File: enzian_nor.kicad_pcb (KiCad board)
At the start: 4 copper layers, 75 x 60 mm, 27 parts, among them IC1 L7809ABD2T-TR, J1 ASP-134488-01, U1 MT35XU02GCBA1G12-0AUT

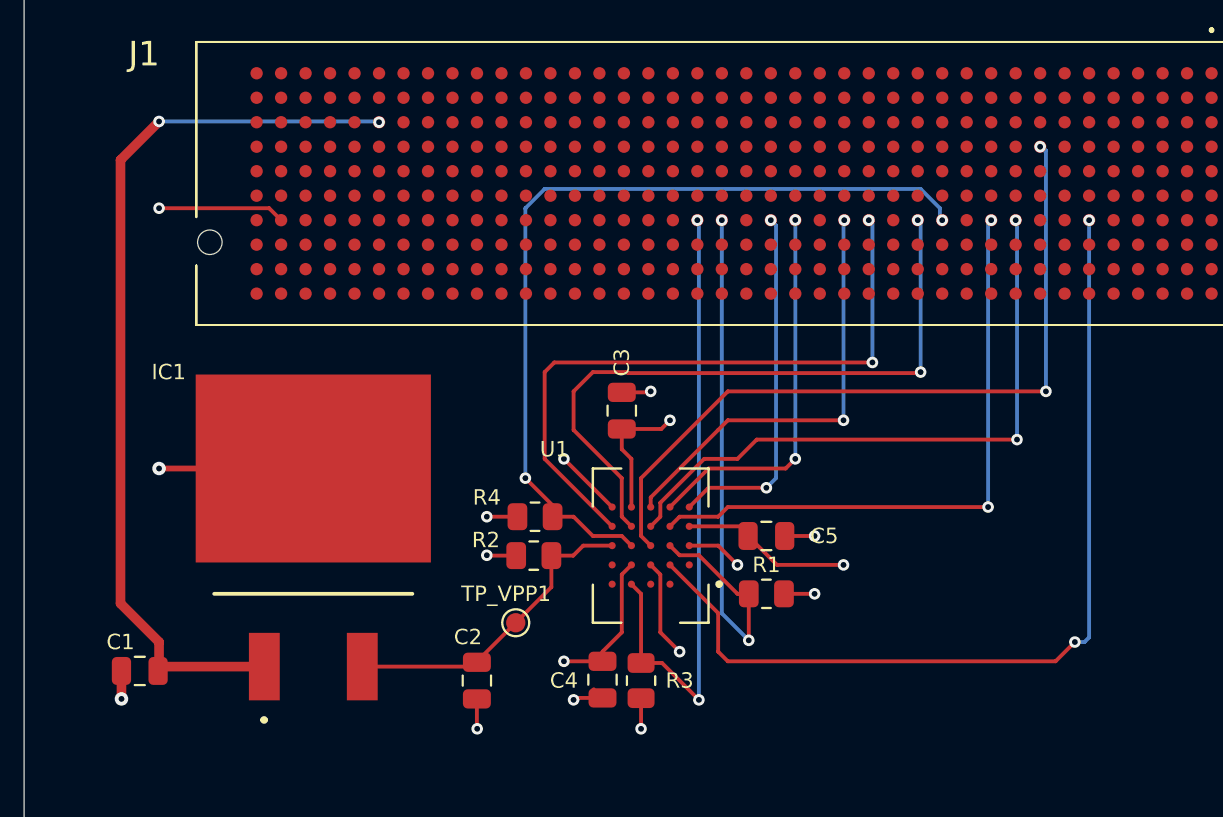
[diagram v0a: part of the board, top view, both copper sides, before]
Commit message: Update vias to diagonal positions to match the enzian main board
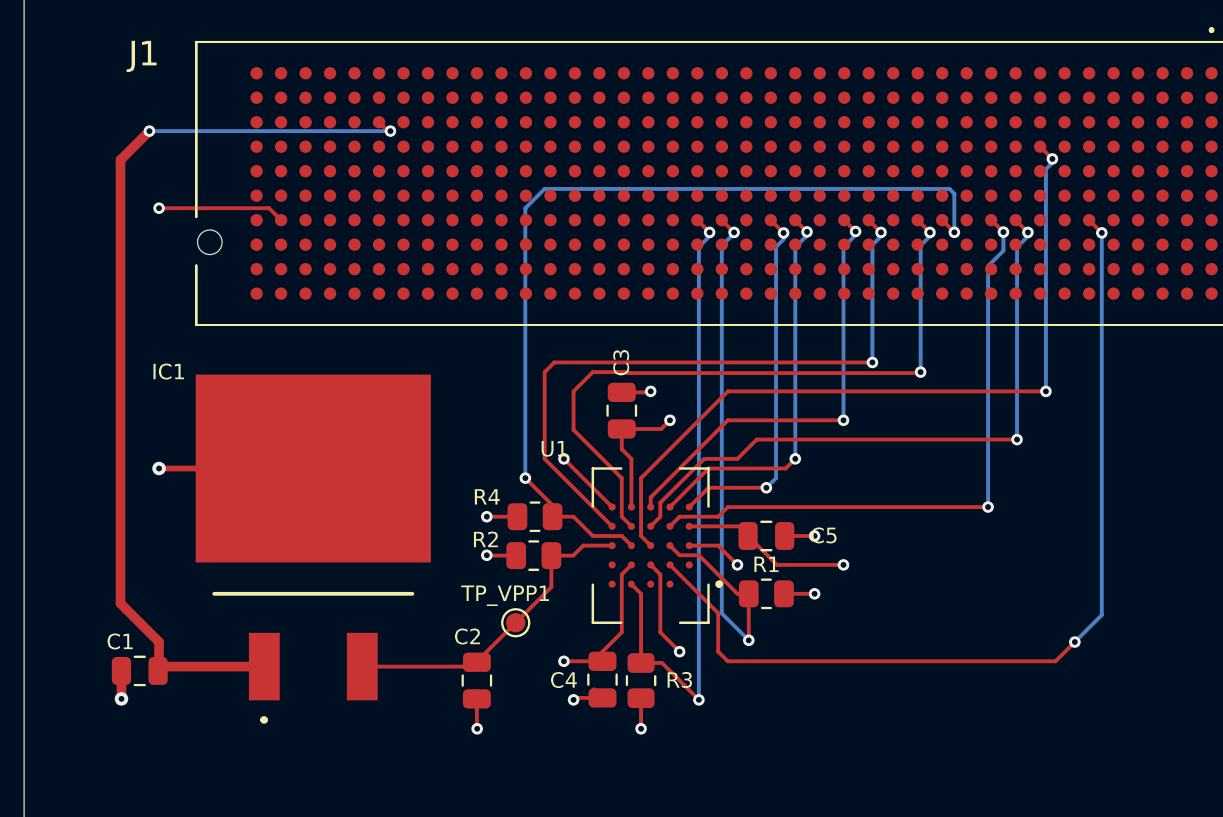
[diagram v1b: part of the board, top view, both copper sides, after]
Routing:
- net /NOR_DQ2: track 44.3 -> 47.1 mm
- net /12V_PSUP: track 47.3 -> 48.4 mm
- net /NOR_DQ1: track 31.9 -> 32.6 mm
- net /NOR_S#: track 30.0 -> 30.6 mm

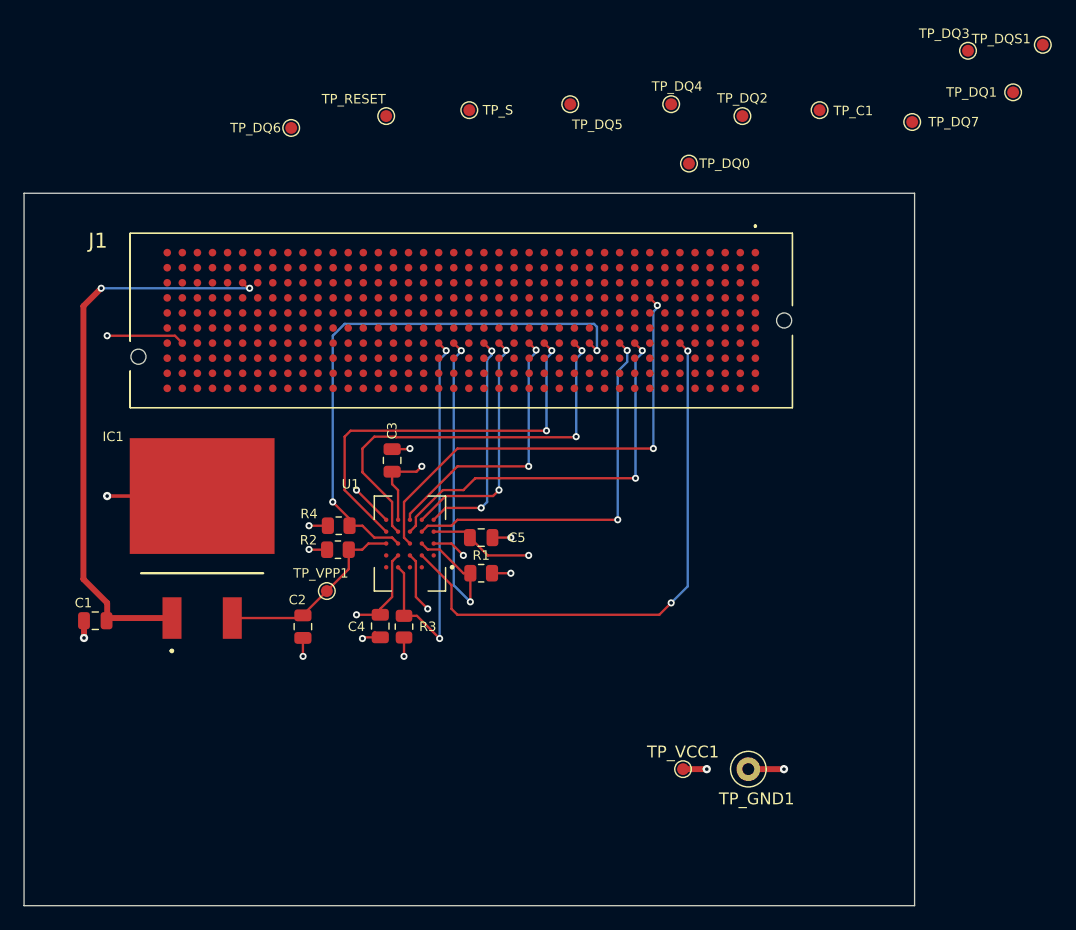
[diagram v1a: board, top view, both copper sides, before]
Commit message: Change trace width to 0.35mm/0.5mm for control/power traces, and connected test pads
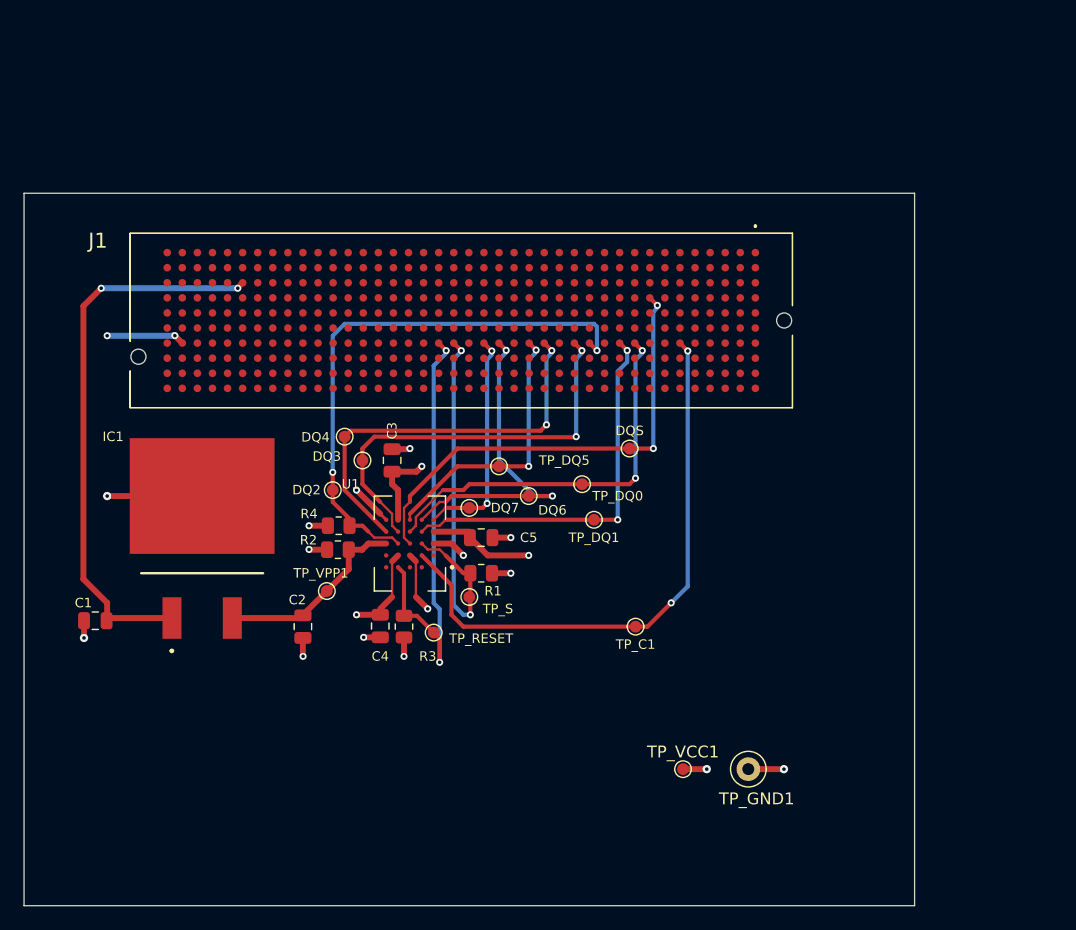
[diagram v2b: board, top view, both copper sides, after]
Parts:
- moved DQ3 61.6 mm to (44.5, 102.0)
- moved TP_DQ1 50.4 mm to (64.0, 107.0)
- moved DQ7 49.5 mm to (53.5, 106.0)
- moved DQS 48.7 mm to (67.0, 101.0)
- moved DQ2 46.7 mm to (42.0, 104.5)
- moved TP_C1 46.2 mm to (67.5, 116.0)
- moved TP_RESET 43.7 mm to (50.5, 116.5)
- moved TP_S 41.0 mm to (53.5, 113.5)
- moved DQ4 39.2 mm to (43.0, 100.0)
- moved DQ6 36.9 mm to (58.5, 105.0)
- moved TP_DQ5 31.1 mm to (56.0, 102.5)
- moved TP_DQ0 28.5 mm to (63.0, 104.0)
- renumbered TP_DQ2 to DQ2, TP_DQ3 to DQ3, TP_DQ4 to DQ4, TP_DQ6 to DQ6, TP_DQ7 to DQ7, TP_DQS1 to DQS
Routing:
- net /NOR_DQ6: track 20.4 -> 28.0 mm
- net /NOR_RESET#: track 33.5 -> 37.9 mm
- net /NOR_S#: track 30.6 -> 34.0 mm
- net /12V_PSUP: track 48.4 -> 47.2 mm
- net /NOR_C: track 47.4 -> 48.5 mm
- net VCC: vias 8 -> 9

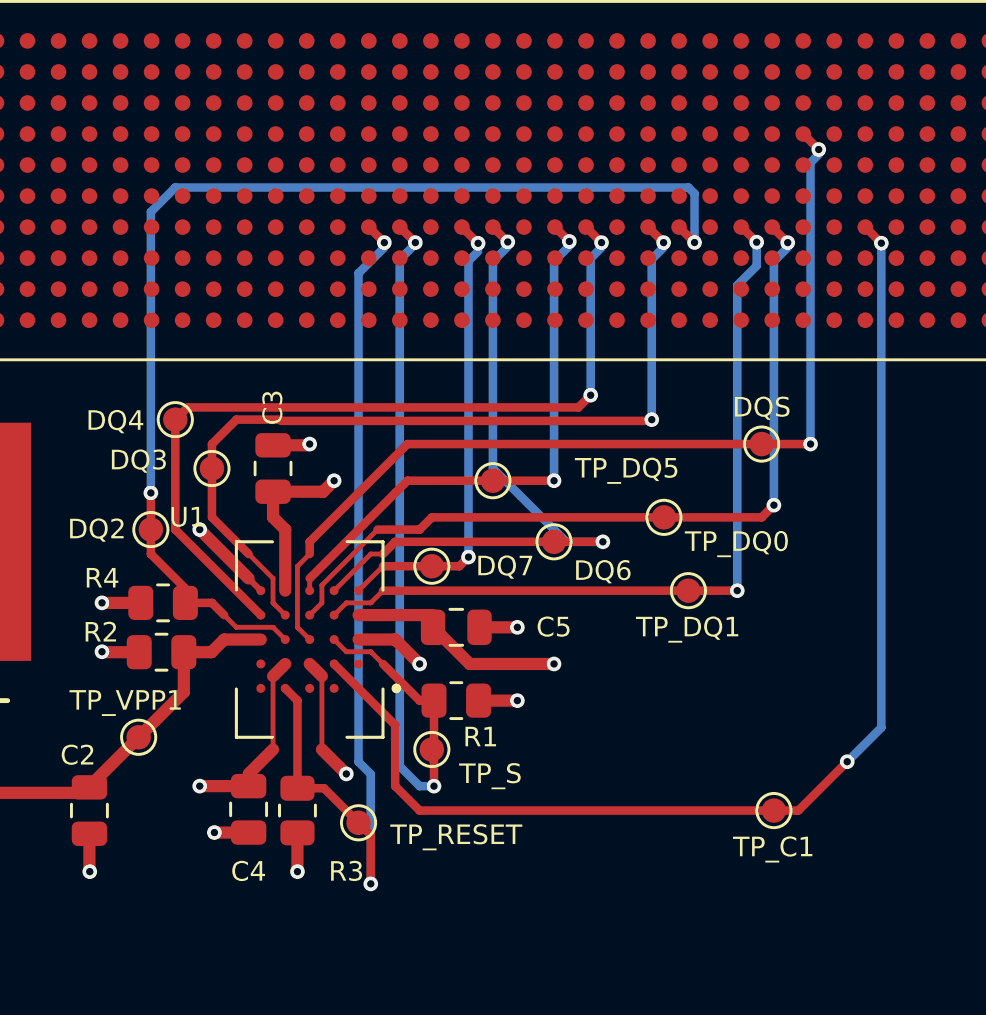
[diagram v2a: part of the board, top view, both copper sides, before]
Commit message: Match trace lengths for all control signals (DQ0-7, C, S#)
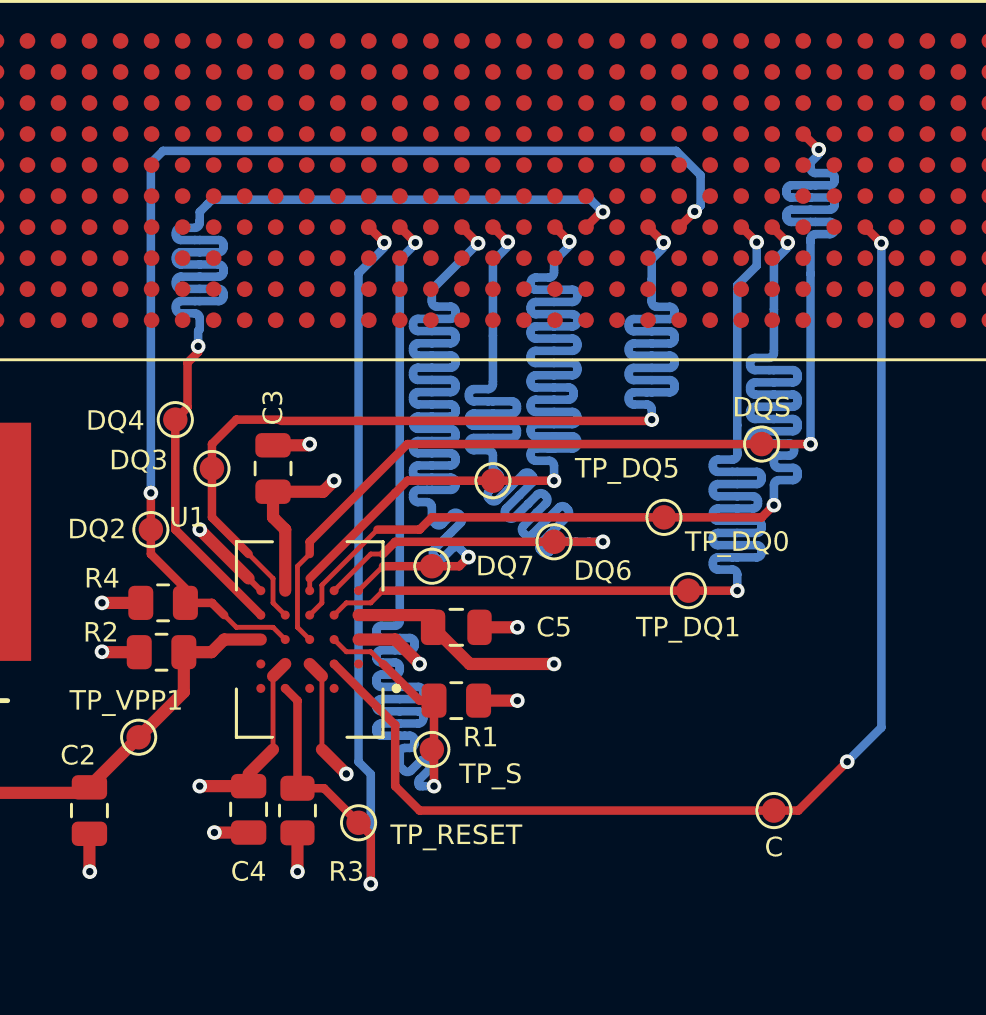
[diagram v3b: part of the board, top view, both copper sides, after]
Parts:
- renumbered TP_C1 to C
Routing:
- net /NOR_DQ7: track 19.0 -> 48.2 mm
- net /NOR_DQ5: track 23.0 -> 48.3 mm
- net /NOR_DQ6: track 28.0 -> 48.3 mm
- net /NOR_DQ1: track 32.6 -> 48.4 mm
- net /NOR_S#: track 34.0 -> 49.3 mm
- net /NOR_DQ0: track 33.2 -> 48.3 mm
- net /NOR_DQ4: track 34.2 -> 48.5 mm
- net /NOR_DQ3: track 35.0 -> 48.4 mm
- net /NOR_DQS: track 39.7 -> 48.4 mm
- net /NOR_DQ2: track 47.1 -> 49.1 mm

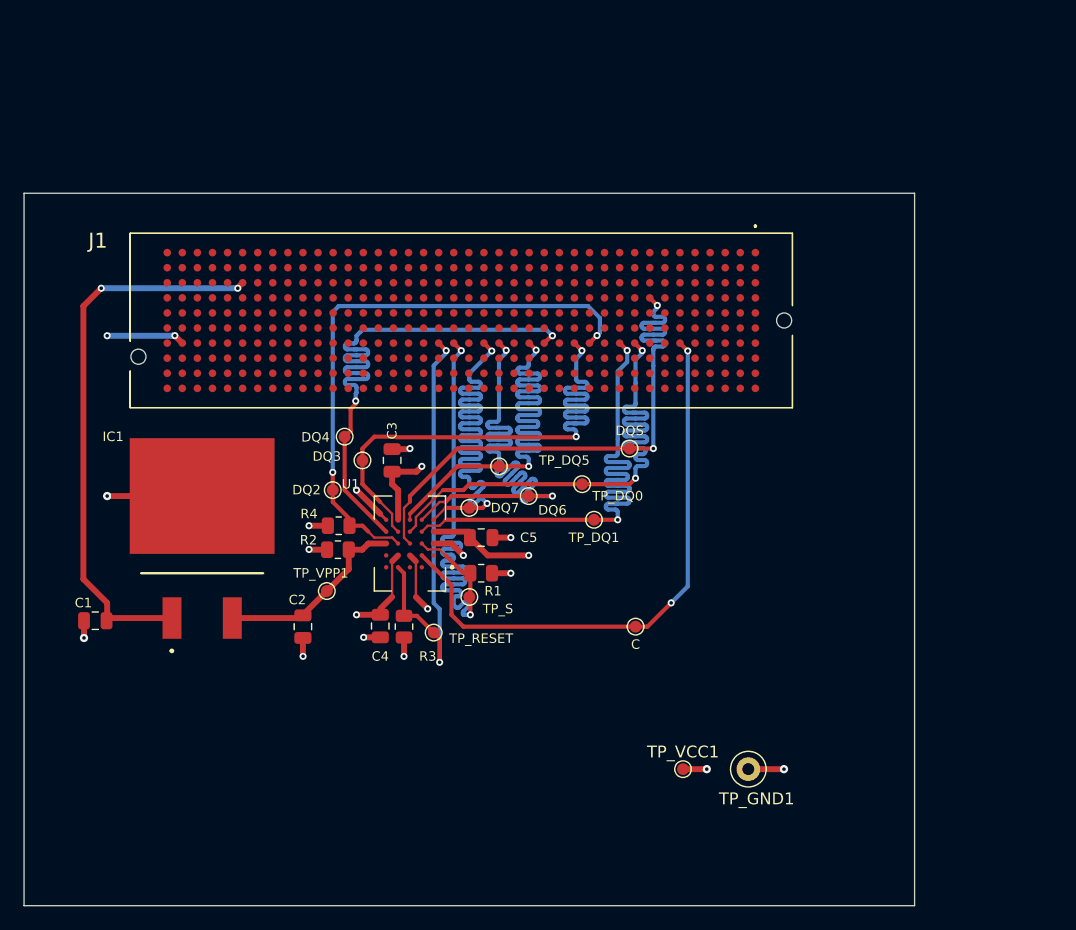
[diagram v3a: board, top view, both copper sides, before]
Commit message: Pour coplanarground plane on the front copper
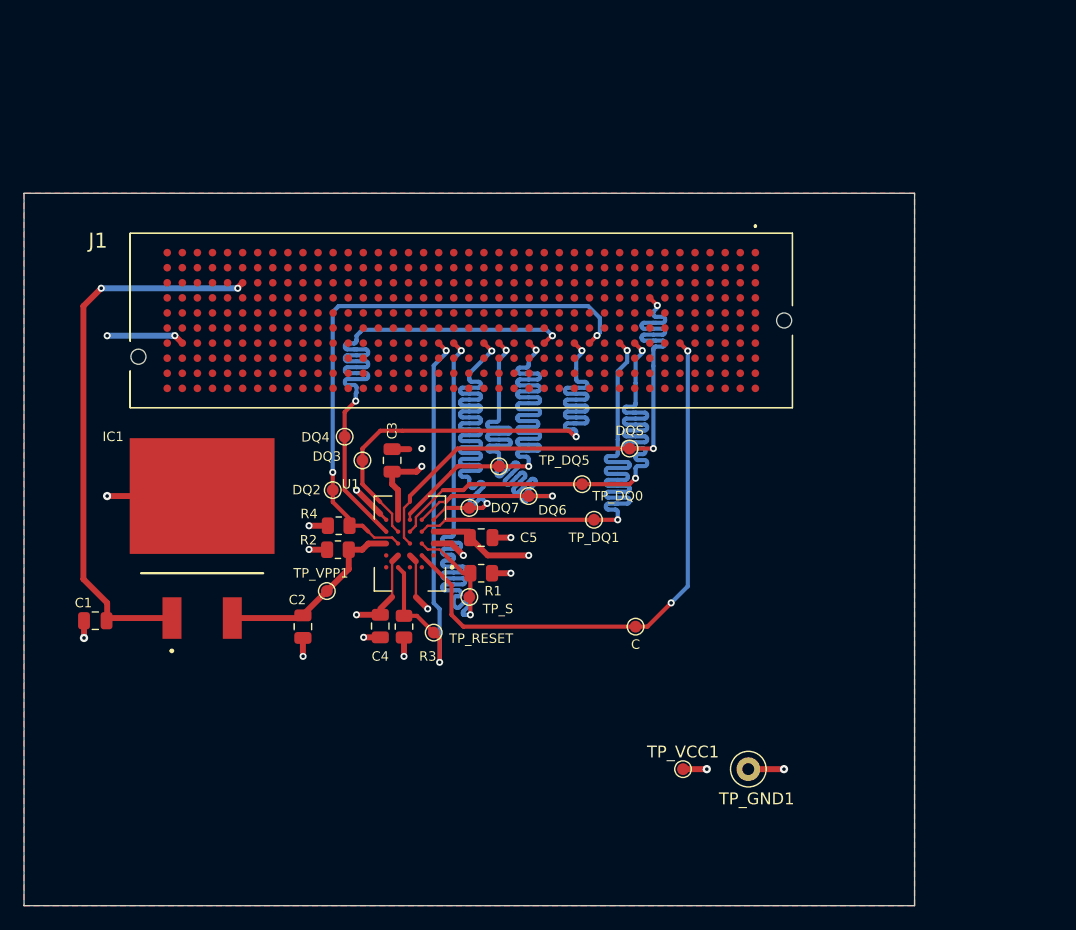
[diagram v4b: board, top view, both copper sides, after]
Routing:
- added copper zone on F.Cu, net GND
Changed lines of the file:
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@@
 	)
 	(segment
-		(start 46 105.5)
-		(end 44.5 104)
+		(start 46 99.5)
+		(end 47.872548 99.5)
 		(width 0.35)
 		(layer "F.Cu")
@@
 	)
 	(segment
-		(start 45.5 100)
-		(end 47.270548 100)
+		(start 61.898 99.5)
+		(end 62.449 100.051)
 		(width 0.35)
 		(layer "F.Cu")
@@
 	)
 	(segment
-		(start 47.270548 100)
-		(end 47.321548 100.051)
+		(start 47 106.5)
+		(end 46 105.5)
 		(width 0.2)
 		(layer "F.Cu")
@@
 	)
 	(segment
-		(start 47.321548 100.051)
-		(end 62.449 100.051)
+		(start 47.872548 99.5)
+		(end 61.898 99.5)
 		(width 0.35)
 		(layer "F.Cu")
@@
 	)
 	(segment
-		(start 44.5 104)
-		(end 44.5 101)
+		(start 44.5 101)
+		(end 46 99.5)
 		(width 0.35)
 		(layer "F.Cu")
@@
 	)
 	(segment
-		(start 47 106.5)
-		(end 46 105.5)
-		(width 0.2)
-		(layer "F.Cu")
-		(net 392)
-	)
-	(segment
-		(start 44.5 101)
-		(end 45.5 100)
+		(start 62.984999 92.754999)
+		(end 62.35 92.12)
 		(width 0.35)
 		(layer "F.Cu")
@@
 	)
 	(segment
-		(start 62.984999 92.754999)
-		(end 62.35 92.12)
+		(start 46 105.5)
+		(end 44.5 104)
 		(width 0.35)
 		(layer "F.Cu")
@@
 	)
 	(segment
+		(start 44.5 104)
+		(end 44.5 101)
+		(width 0.35)
+		(layer "F.Cu")
+		(net 392)
+	)
+	(segment
 		(start 62.449 100.051)
 		(end 62.5 100)
@@
 	)
 	(segment
+		(start 43.935001 97)
+		(end 43 97.935001)
+		(width 0.35)
+		(layer "F.Cu")
+		(net 403)
+	)
+	(segment
 		(start 60.43 91.5)
 		(end 59.81 92.12)
@@
 	)
 	(segment
-		(start 43.5 99.5)
+		(start 43 97.935001)
 		(end 43 100)
 		(width 0.35)
@@
 		(net 403)
 	)
-	(segment
-		(start 43.5 97.670404)
-		(end 43.5 99.5)
-		(width 0.35)
-		(layer "F.Cu")
-		(net 403)
-	)
-	(segment
-		(start 43.935001 97.235403)
-		(end 43.5 97.670404)
-		(width 0.35)
-		(layer "F.Cu")
-		(net 403)
-	)
-	(segment
-		(start 43.935001 97)
-		(end 43.935001 97.235403)
-		(width 0.35)
-		(layer "F.Cu")
-		(net 403)
-	)
 	(via
 		(at 60.5 91.5)
@@
 	)
 	(via
-		(at 48.5 101)
-		(size 0.6)
-		(drill 0.3)
-		(layers "F.Cu" "B.Cu")
-		(net 406)
-	)
-	(via
 		(at 21.05 116.95)
 		(size 0.7)
@@
 		(net 406)
 	)
+	(via
+		(at 49.5 101)
+		(size 0.6)
+		(drill 0.3)
+		(layers "F.Cu" "B.Cu")
+		(free yes)
+		(net 406)
+	)
 	(segment
 		(start 39.259969 115.275)
@@
 	)
 	(zone
+		(net 406)
+		(net_name "GND")
+		(layer "F.Cu")
+		(hatch edge 0.5)
+		(priority 2)
+		(connect_pads
+			(clearance 0.7)
+		)
+		(min_thickness 0.15)
+		(filled_areas_thickness no)
+		(fill yes
+			(thermal_gap 0.5)
+			(thermal_bridge_width 0.5)
+		)
+		(polygon
+			(pts
+				(xy 16 79.5) (xy 16 139.5) (xy 91 139.5) (xy 91 79.5)
+			)
+		)
+	)
+	(zone
